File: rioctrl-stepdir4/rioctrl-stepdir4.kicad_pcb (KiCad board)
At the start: 2 copper layers, 100 x 100 mm, 93 parts, among them J1 Conn_02x13_Odd_Even, J2 RJ45_LED_Shielded, J3 RJ45_LED_Shielded, J4 RJ45_LED_Shielded, J5 RJ45_LED_Shielded, Q1 BSS138W, Q10 AO3401A, Q11 BSS138W, Q12 AO3401A, Q2 BSS138W, Q3 AO3401A, Q4 AO3401A, Q5 BSS138W, Q6 AO3401A, Q7 BSS138W, Q8 AO3401A, Q9 BSS138W, U1 CS48505S, U10 CS48505S, U11 CS48505S, U12 USBLC6-4SC6, U2 CS48505S, U3 USBLC6-4SC6, U4 CS48505S, U5 CS48505S, U6 USBLC6-4SC6, U7 CS48505S, U8 CS48505S, U9 USBLC6-4SC6

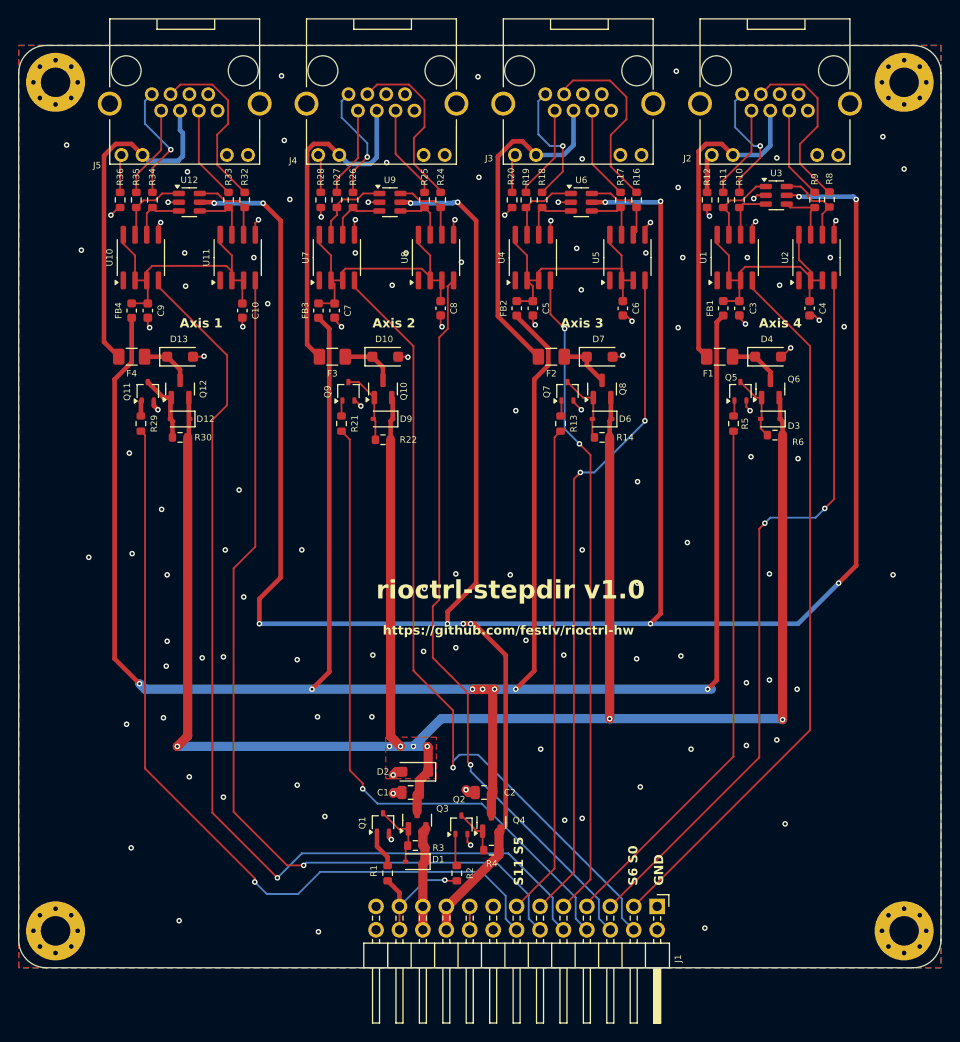
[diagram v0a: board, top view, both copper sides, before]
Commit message: Add forgotten series resistor for 24V output transistors in rioctrl-stepdir4
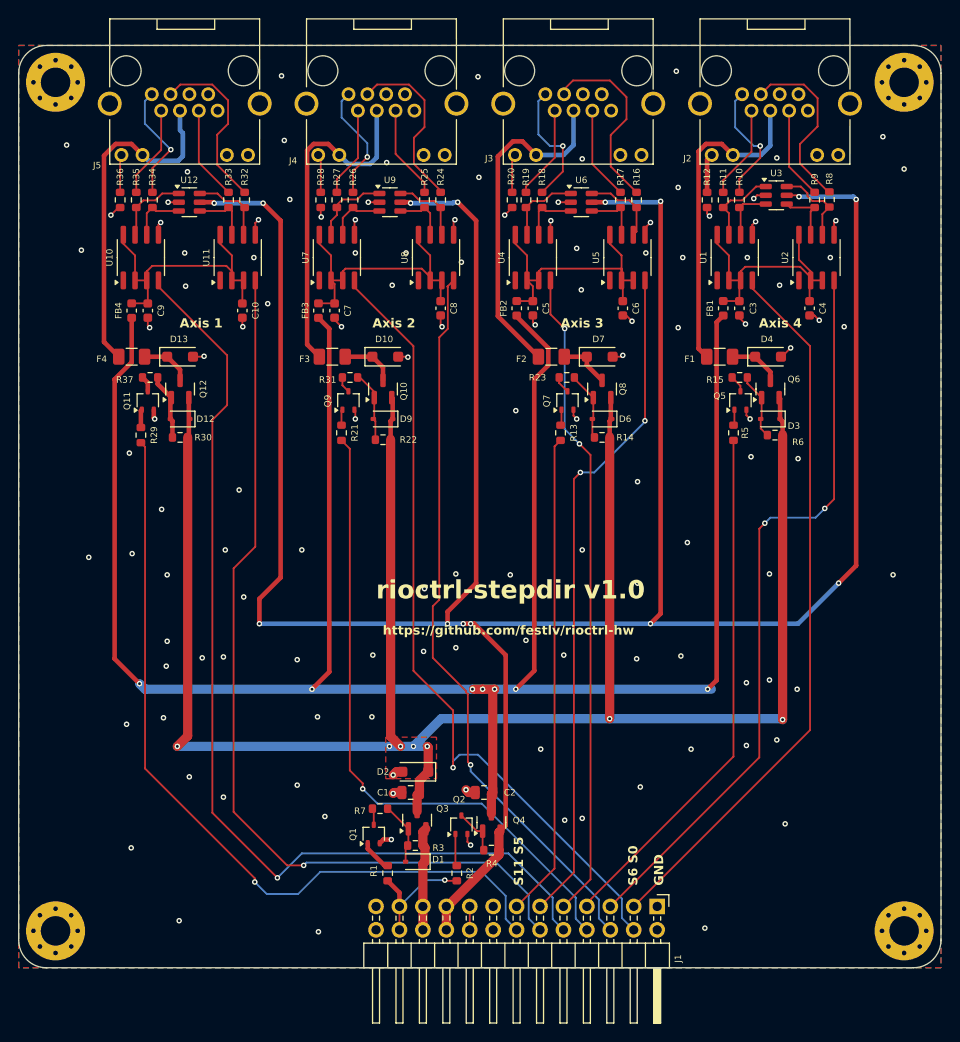
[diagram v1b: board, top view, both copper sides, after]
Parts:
- added R15: 10K, Resistor_SMD:R_0603_1608Metric, F.Cu at (153.2, 91.0)
- added R23: 10K, Resistor_SMD:R_0603_1608Metric, F.Cu at (134.4, 91.0)
- added R31: 10K, Resistor_SMD:R_0603_1608Metric, F.Cu at (110.9, 91.0)
- added R37: 10K, Resistor_SMD:R_0603_1608Metric, F.Cu at (89.2, 91.0)
- added R7: 10K, Resistor_SMD:R_0603_1608Metric, F.Cu at (114.2, 137.8)
- moved Q1 1.60 mm to (113.5, 140.5)
- moved R29 1.25 mm to (88.2, 97.2)
- moved Q11 1.00 mm to (89.0, 93.5)
- moved Q5 1.00 mm to (153.2, 93.5)
- moved Q7 1.00 mm to (134.5, 93.5)
- moved Q9 1.00 mm to (110.8, 93.5)
- moved R13 1.00 mm to (133.8, 97.0)
- moved R21 1.00 mm to (110.0, 97.0)
- moved R5 1.00 mm to (152.5, 97.0)
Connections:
- Q1 pad 3: Net-(D1-A) -> Net-(Q1-D)
- Q11 pad 3: Net-(D12-A) -> Net-(Q11-D)
- Q5 pad 3: Net-(D3-A) -> Net-(Q5-D)
- Q7 pad 3: Net-(D6-A) -> Net-(Q7-D)
- Q9 pad 3: Net-(D9-A) -> Net-(Q9-D)
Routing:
- net Net-(Q7-D): track 0.00 -> 1.87 mm
- net Net-(Q5-D): track 0.00 -> 1.87 mm
- net Net-(Q1-D): track 0.00 -> 1.81 mm
- net Net-(Q9-D): track 0.00 -> 1.77 mm
- net Net-(Q11-D): track 0.00 -> 1.74 mm
- net /Slot input/S11: track 88.0 -> 86.7 mm
- net /Slot input/S5: track 53.5 -> 52.5 mm
- net /Slot input/S8: track 71.7 -> 70.7 mm
- net /Slot input/S2: track 58.1 -> 57.1 mm
- net Net-(Q1-G): track 4.15 -> 3.51 mm

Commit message: Release rioctrl-stepdir v1.1
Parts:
- moved J1 4.00 mm to (140.2, 148.3)
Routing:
- net /Slot input/SlotEN: track 13.3 -> 19.5 mm
- net /Slot input/S0: track 78.4 -> 82.8 mm
- net /Slot input/S1: track 80.8 -> 85.0 mm
- net /Slot input/S9: track 108.4 -> 104.3 mm
- net +5V: track 315.4 -> 319.4 mm
- net /Slot input/S10: track 98.9 -> 95.1 mm
- net /Slot input/S2: track 57.1 -> 60.9 mm
- net /Slot input/S11: track 86.7 -> 83.3 mm
- net GND: track 47.5 -> 50.0 mm, vias 125 -> 126
- net /Slot input/S7: track 79.4 -> 77.7 mm
- net /Slot input/S5: track 52.5 -> 54.2 mm
- net /Slot input/S8: track 70.7 -> 69.0 mm
- net +24V: track 11.3 -> 12.9 mm
- net /Slot input/S4: track 73.6 -> 75.3 mm
- net /Slot input/S3: track 70.9 -> 72.5 mm
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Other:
- board text added: "Joint 0"
- board text added: "Joint 1"
- board text added: "Joint 2"
- board text added: "Joint 3"
- board text added: "rioctrl-stepdir v1.1"
- board text removed: "Axis 1"
- board text removed: "Axis 2"
- board text removed: "Axis 3"
- board text removed: "Axis 4"
- board text removed: "rioctrl-stepdir v1.0"
